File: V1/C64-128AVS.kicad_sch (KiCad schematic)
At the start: 11 parts, among them J1 RTC9028, J10 Conn_01x02, J2 SV80, J3 RCJ-021, J4 RCJ-023, J5 RCJ-022, J6 RCJ-024, J7 Audio IN, J8 Stereo, J9 ChromaFix

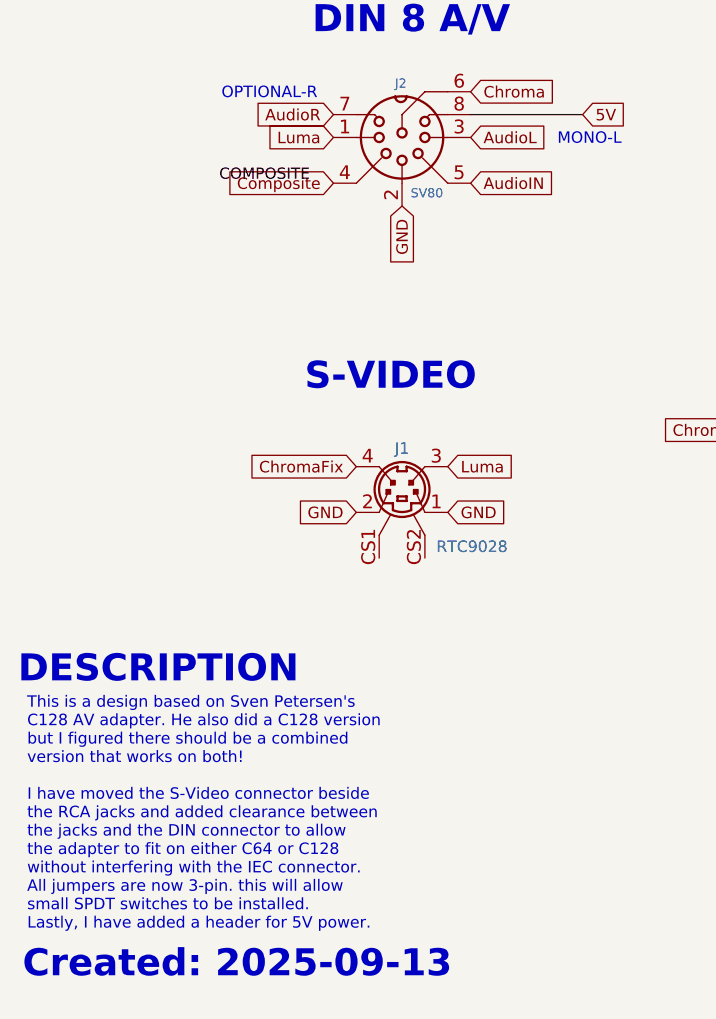
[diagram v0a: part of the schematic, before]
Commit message: Update schematic and add BOM
Updated schematic to add working status. Add interactive BOM.
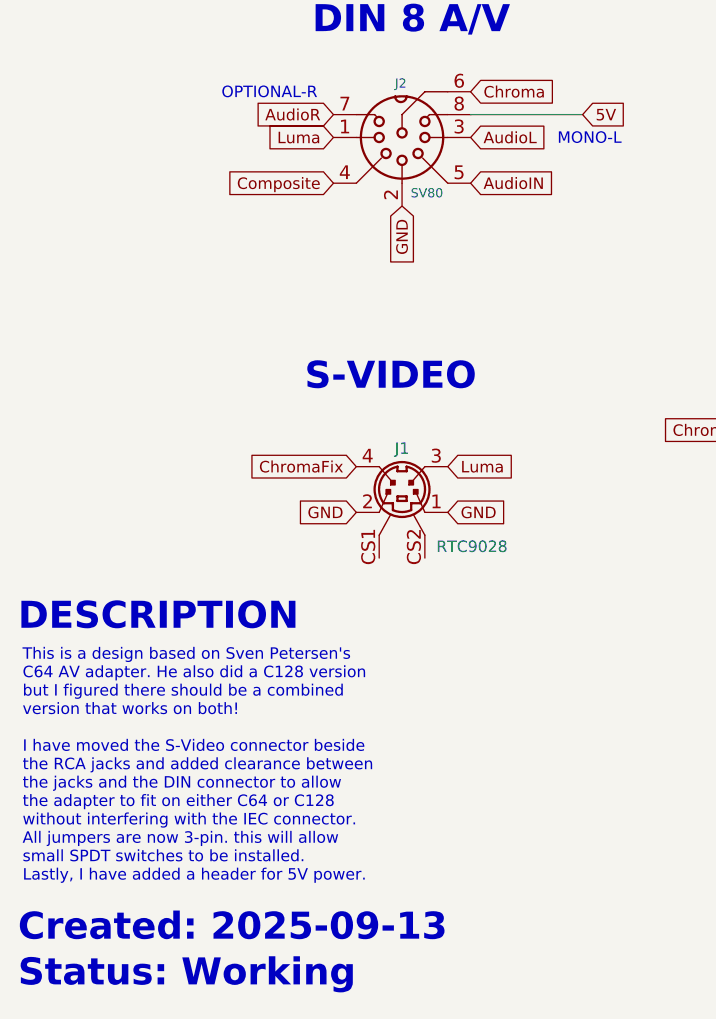
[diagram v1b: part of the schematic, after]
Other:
- note added: "Status: Working"
- note added: "This is a design based on Sven Petersen's C64 AV adapter. He also did a C128 version but I figured there should be a combined version that works on both! I have moved the S-Video connector beside the RCA jacks and added clearance between the jacks and the DIN connector to allow the adapter to fit on either C64 or C128 without interfering with the IEC connector. All jumpers are now 3-pin. this wil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"
- note removed: "This is a design based on Sven Petersen's C128 AV adapter. He also did a C128 version but I figured there should be a combined version that works on both! I have moved the S-Video connector beside the RCA jacks and added clearance between the jacks and the DIN connector to allow the adapter to fit on either C64 or C128 without interfering with the IEC connector. All jumpers are now 3-pin. this wi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"
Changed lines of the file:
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@@
 		)
 	)
-	(text "This is a design based on Sven Petersen's\nC128 AV adapter. He also did a C128 version\nbut I figured there should be a combined\nversion that works on both!\n\nI have moved the S-Video connector beside\nthe RCA jacks and added clearance between\nthe jacks and the DIN connector to allow\nthe adapter to fit on either C64 or C128\nwithout interfering with the IEC connector.\nAll jumpers are now 3-pin. this will allow\nsmall SPDT switches to be installed.\nLastly, I have added a header for 5V power."
-		(exclude_from_sim no)
-		(at 15.494 114.808 0)
+	(text "This is a design based on Sven Petersen's\nC64 AV adapter. He also did a C128 version\nbut I figured there should be a combined\nversion that works on both!\n\nI have moved the S-Video connector beside\nthe RCA jacks and added clearance between\nthe jacks and the DIN connector to allow\nthe adapter to fit on either C64 or C128\nwithout interfering with the IEC connector.\nAll jumpers are now 3-pin. this will allow\nsmall SPDT switches to be installed.\nLastly, I have added a header for 5V power."
+		(exclude_from_sim no)
+		(at 14.986 109.474 0)
 		(effects
 			(font
@@
 	(text "Created: 2025-09-13"
 		(exclude_from_sim no)
-		(at 14.986 131.572 0)
+		(at 14.478 127.508 0)
 		(effects
 			(font
@@
 				(size 1.27 1.27)
 			)
+		)
+	)
+	(text "Status: Working"
+		(exclude_from_sim no)
+		(at 14.478 132.588 0)
+		(effects
+			(font
+				(size 3 3)
+				(thickness 0.6)
+				(bold yes)
+			)
+			(justify left)
 		)
 	)
@@
 	(text "DESCRIPTION"
 		(exclude_from_sim no)
-		(at 14.478 98.806 0)
+		(at 14.478 92.964 0)
 		(effects
 			(font
@@
 		)
 	)
-	(label "COMPOSITE"
-		(at 36.83 44.704 0)
-		(effects
-			(font
-				(size 1.2446 1.2446)
-			)
-			(justify left bottom)
-		)
-	)
